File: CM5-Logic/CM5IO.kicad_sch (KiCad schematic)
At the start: 9 parts, among them J12 1366008, J2 B2B-PH-K-S, J3 B2B-PH-K-S, J4 VR10S09, J6 691210910006, J7 691210910006

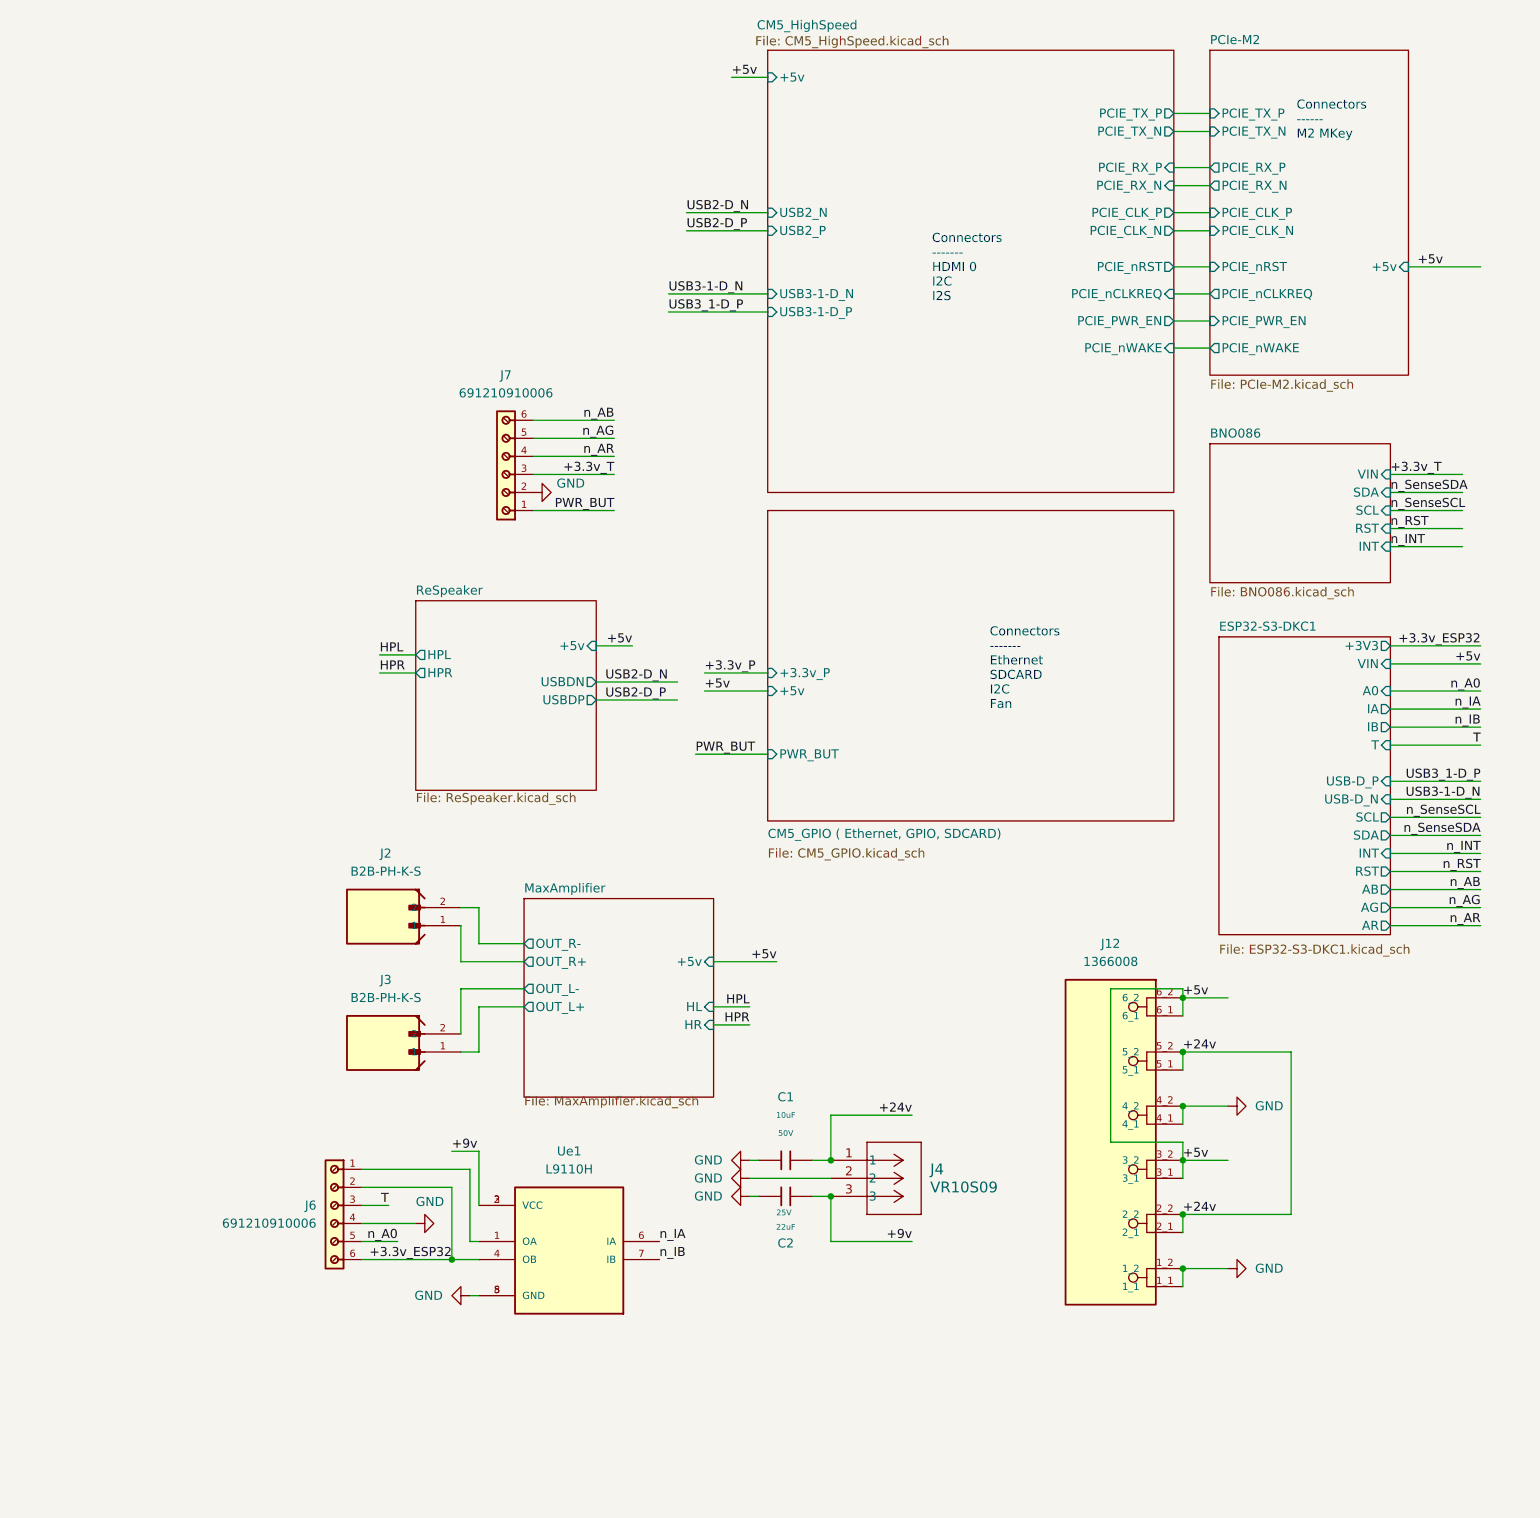
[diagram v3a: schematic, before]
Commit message: adds a base motor driver with UART integration for the ESP32-S3-DC1 base hub
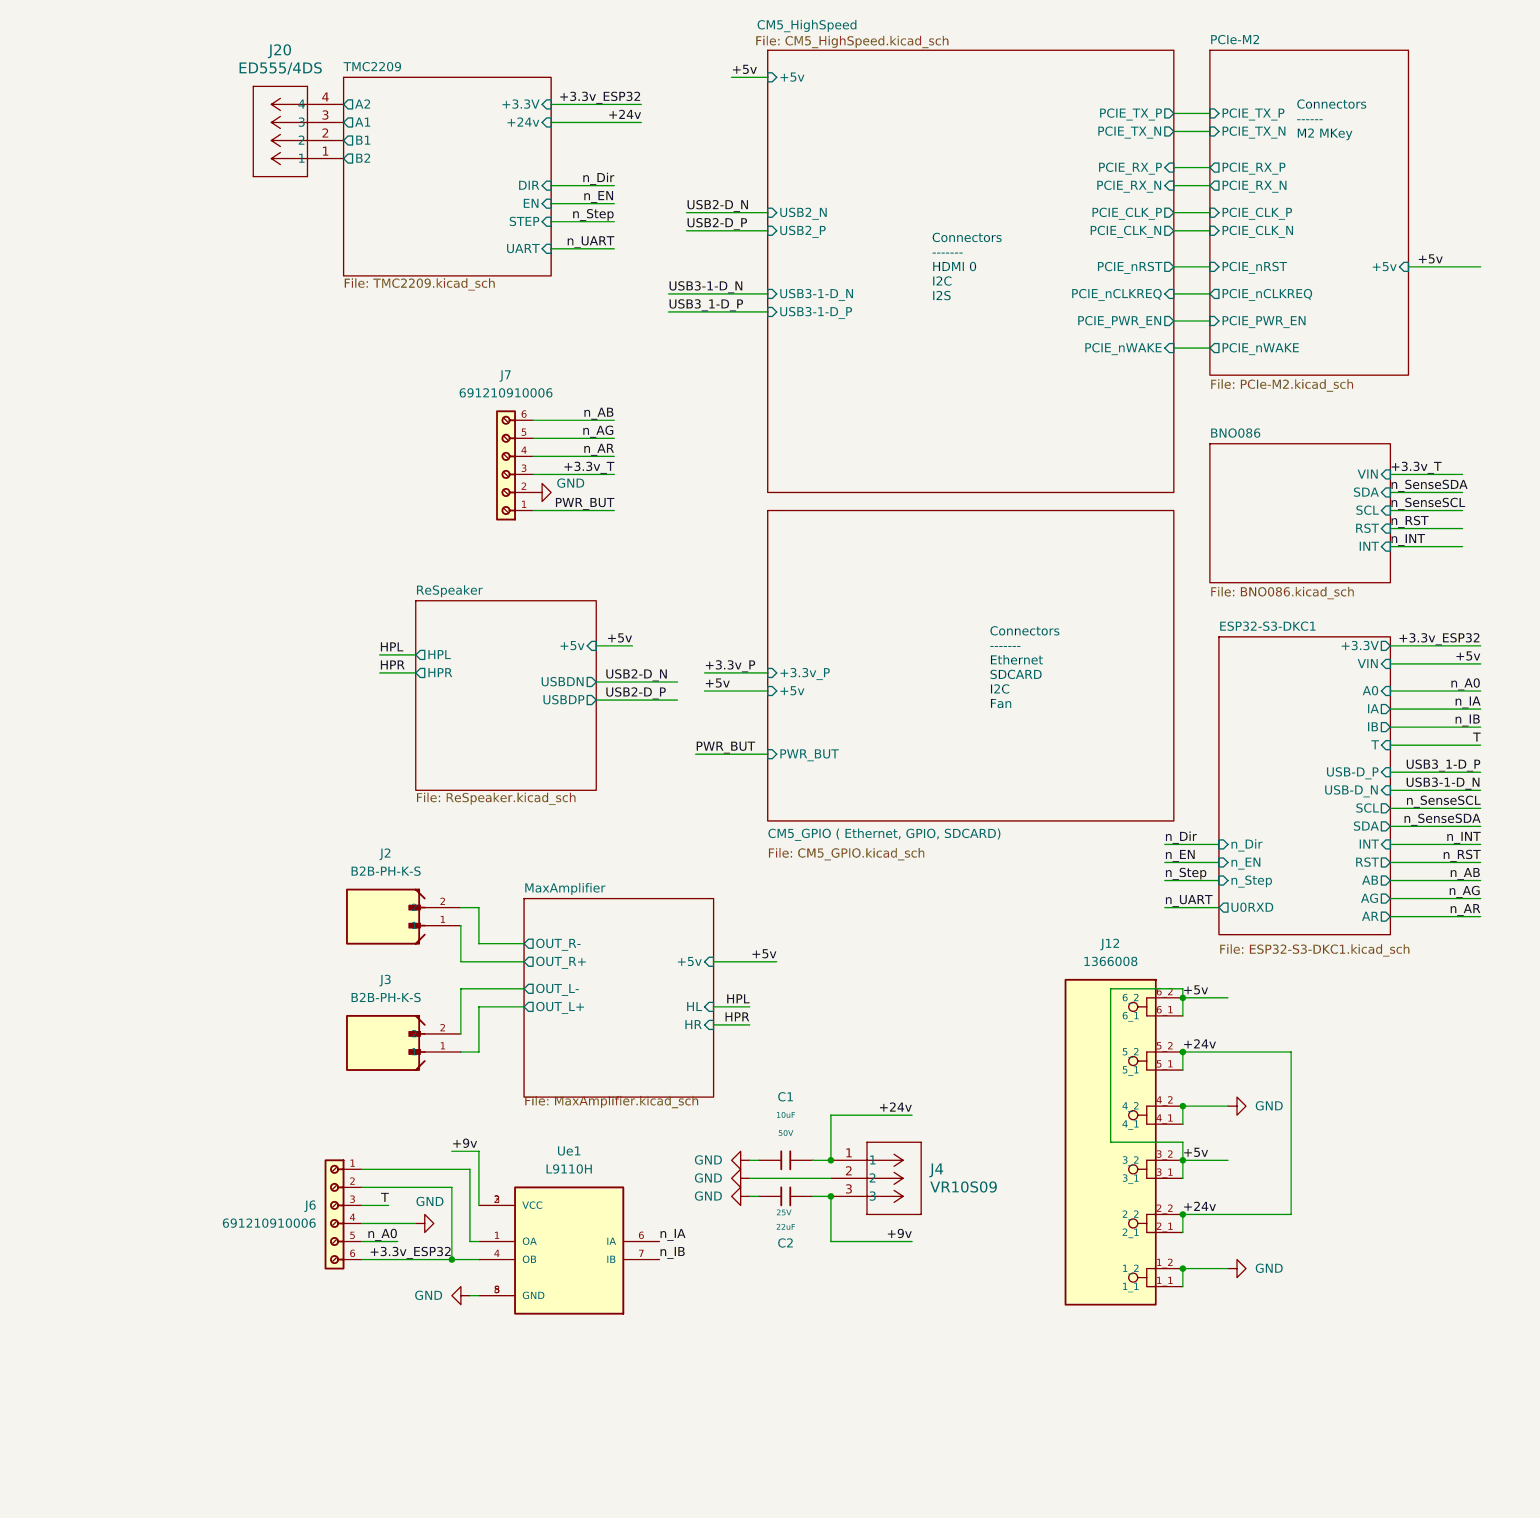
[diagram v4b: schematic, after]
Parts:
- added J20: ED555/4DS, Custom Components:CONN4_ED555&slash_4DS_SHT, symbol CONN4_ED555&slash_4DS_SHT:ED555_4DS
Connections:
- new net TMC2209/A1: J20.3
- new net TMC2209/A2: J20.4
- new net TMC2209/B1: J20.2
- new net TMC2209/B2: J20.1
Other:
- added sheet TMC2209 (TMC2209.kicad_sch)
- sheet ESP32-S3-DKC1 ports: added +3.3V, U0RXD, n_Dir, n_EN, n_Step; removed +3V3

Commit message: adds a 24Pin ATX PSU interface for power and cleans up the amplifier hierarchy
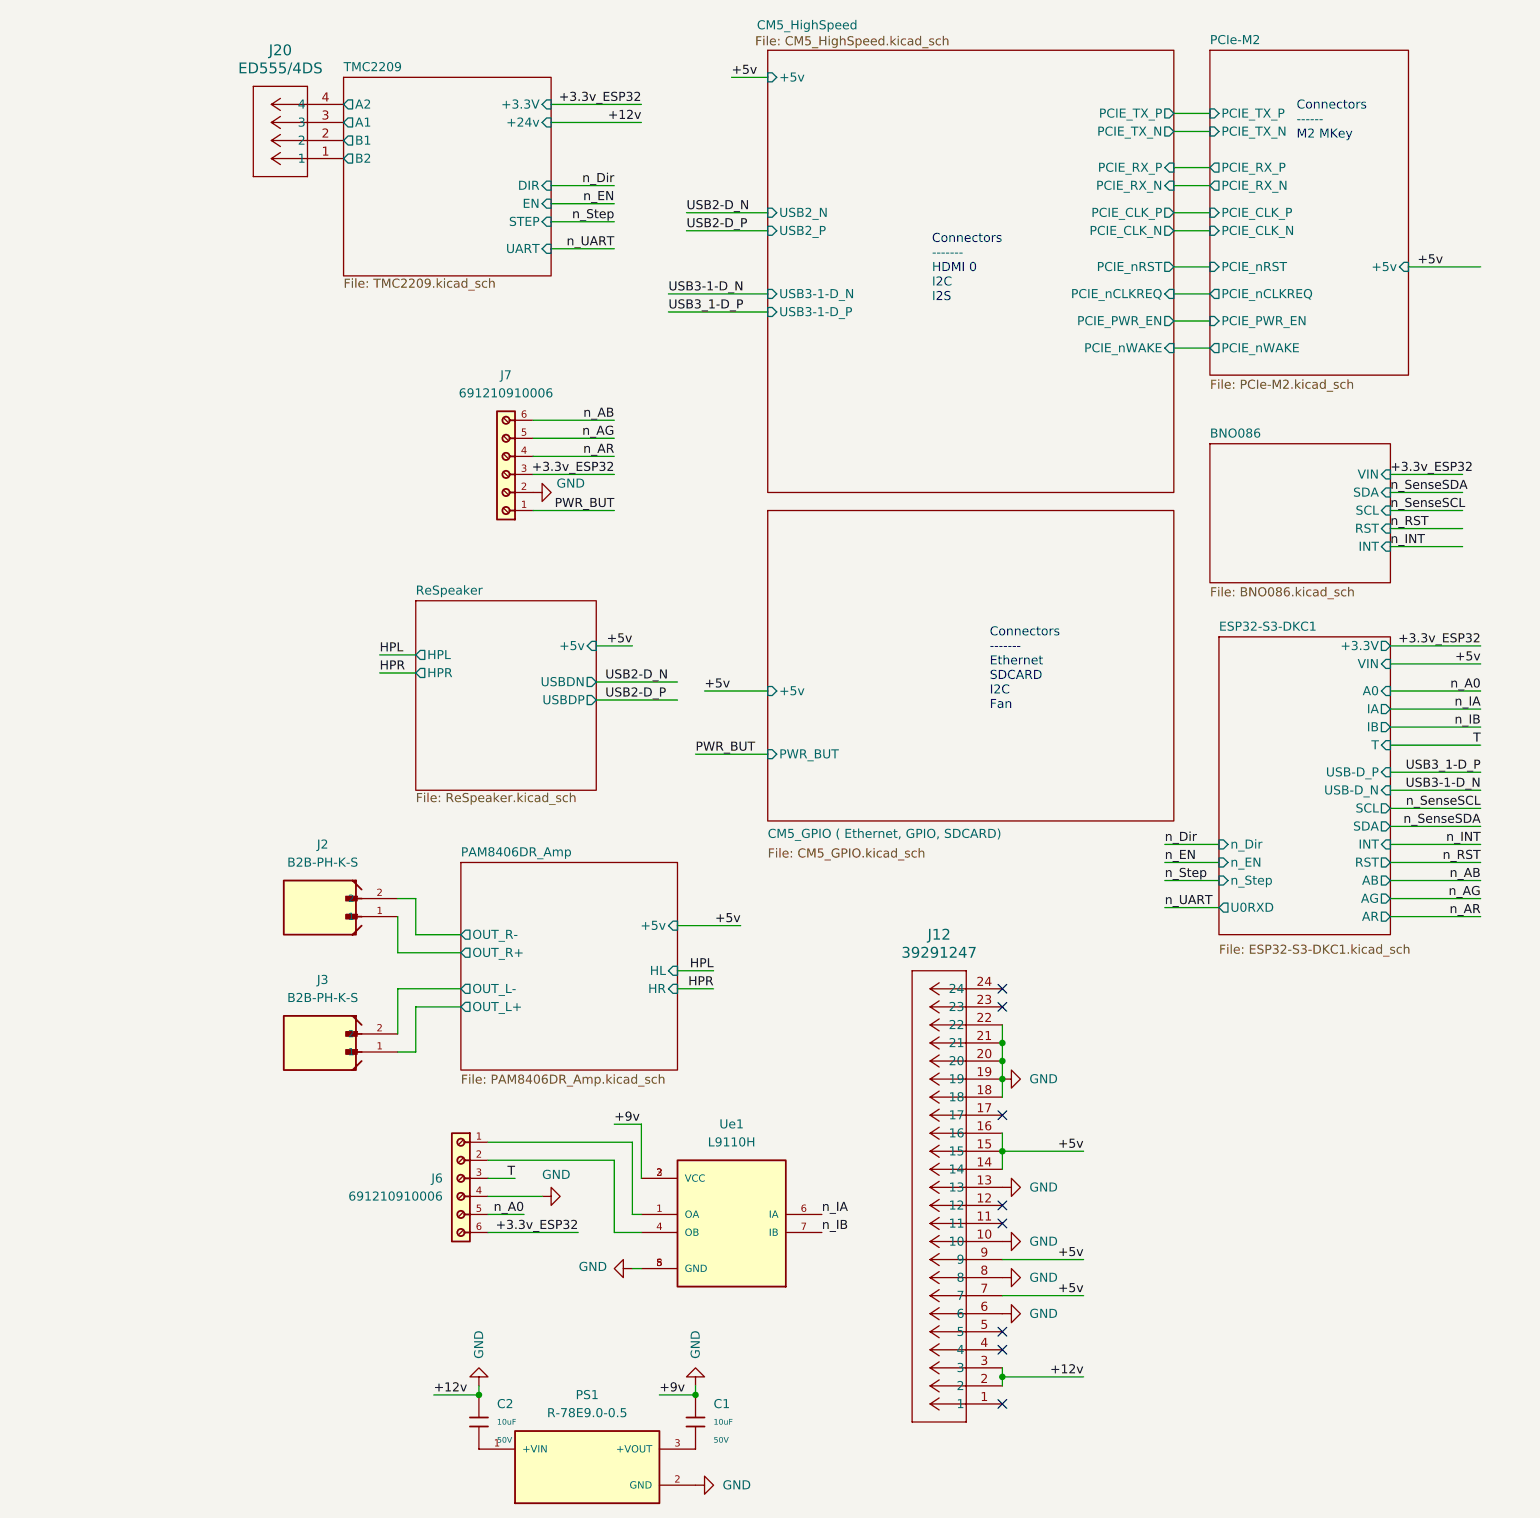
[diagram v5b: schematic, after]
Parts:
- removed C2: 22uF, PCM_JLCPCB:C_0805, symbol PCM_JLCPCB-Capacitors:0805,22uF
- removed J12: 1366008, 1366008:PHOENIX_1366008, symbol 1366008:1366008
- removed J4: VR10S09, Custom Components:VR10S09, symbol VR10S09:VR10S09
- added C2: 10uF, PCM_JLCPCB:C_1206, symbol PCM_JLCPCB-Capacitors:1206,10uF
- added J12: 39291247, CONN_SD-5569-002_24_MOL, symbol CONN_SD-5569-002_24_MOL:39291247
- added PS1: R-78E9.0-0.5, R-78E9.0-0.5:CONV_R-78E9.0-0.5, symbol R-78E9.0-0.5:R-78E9.0-0.5
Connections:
- net +24v is gone; now on net GND: C1.2
- net +3.3v_T is gone; now on net +3.3v_ESP32: J7.3
- net +9v is gone; now on net GND: Ue1.2 (VCC), Ue1.3 (VCC)
- net +3.3v_ESP32: no longer J6.2, Ue1.4 (OB)
- net +5v: now also J12.14, J12.15, J12.16, J12.7, J12.9
- net GND: now also C2.2, J12.10, J12.13, J12.18, J12.19, J12.2, J12.20, J12.21, J12.22, J12.3, J12.6, J12.8, PS1.2 (GND); no longer C1.1
- net MaxAmplifier/OUT_L+ renamed PAM8406DR_Amp/OUT_L+
- net MaxAmplifier/OUT_L- renamed PAM8406DR_Amp/OUT_L-
- net MaxAmplifier/OUT_R+ renamed PAM8406DR_Amp/OUT_R+
- net MaxAmplifier/OUT_R- renamed PAM8406DR_Amp/OUT_R-
- new net: C1.1, PS1.3 (+VOUT)
- new net: J6.2, Ue1.4 (OB)
- new net: C2.1, PS1.1 (+VIN)
- no-connect marks 0 -> 8
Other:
- removed sheet MaxAmplifier
- added sheet PAM8406DR_Amp (PAM8406DR_Amp.kicad_sch)
- sheet CM5_GPIO ( Ethernet, GPIO, SDCARD) ports: added none; removed +3.3v_P
- moved on the sheet: C1, J2, J3, J6, Ue1

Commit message: adds the 8-PIN PSU EPS connction for higher available current on the CM5 Carrier board
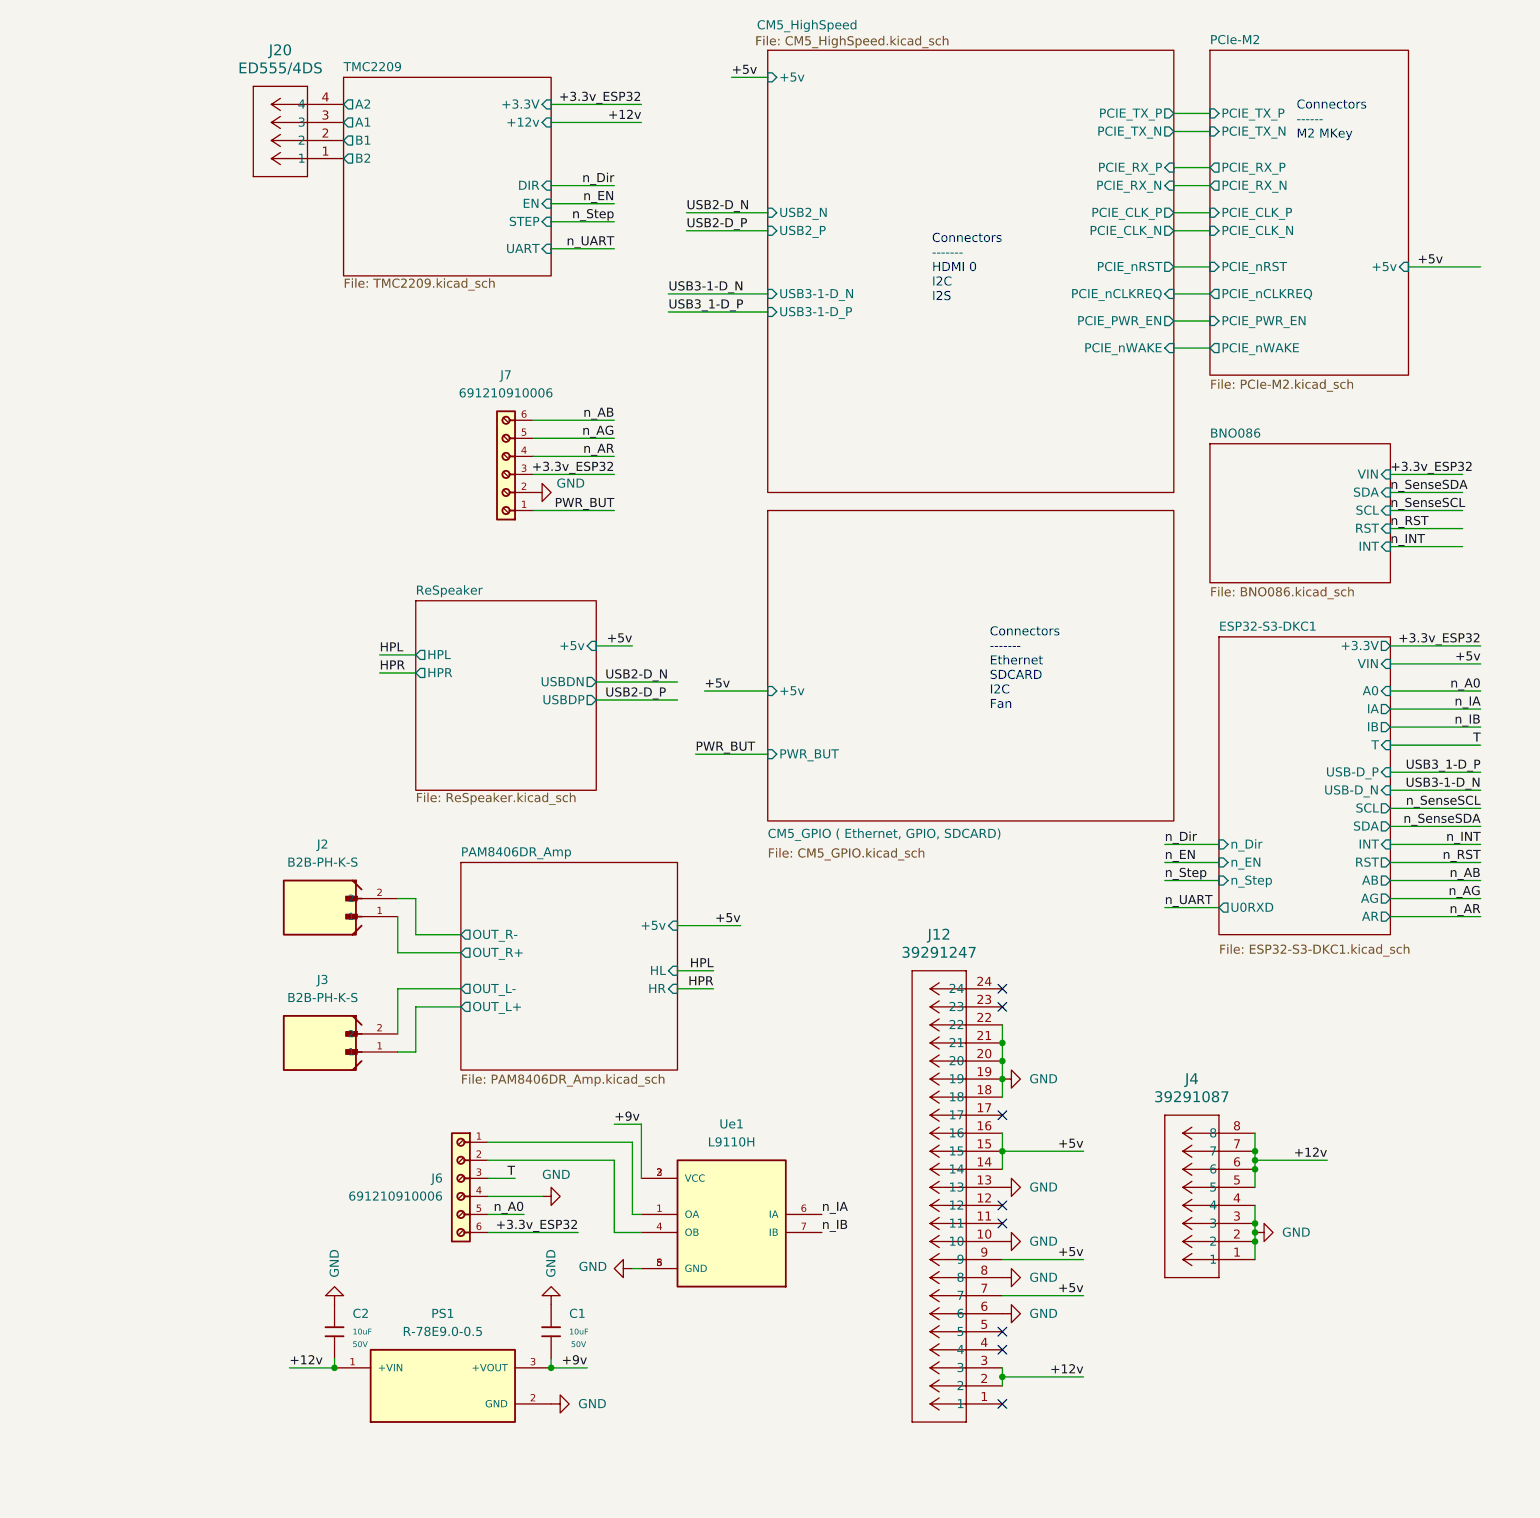
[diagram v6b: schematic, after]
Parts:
- added J4: 39291087, Custom Components:CONN_SD-5569-002_08_MOL, symbol CONN_SD-5569-002_08_MOL:39291087
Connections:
- net GND: now also J4.1, J4.2, J4.3, J4.4; no longer J12.2, J12.3, Ue1.2 (VCC), Ue1.3 (VCC)
- net +9v: now reaches C1.1, PS1.3 (+VOUT)
- net +9v: now also Ue1.2 (VCC), Ue1.3 (VCC)
- net +12v: now reaches C2.1, PS1.1 (+VIN)
- net +12v: now also J12.2, J12.3, J4.5, J4.6, J4.7, J4.8
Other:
- sheet TMC2209 ports: added +12v; removed +24v
- moved on the sheet: C1, C2, PS1
